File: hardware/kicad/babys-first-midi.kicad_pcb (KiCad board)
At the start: 2 copper layers, 100 x 70 mm, 26 parts, among them J1 BFM:RJ45_THT, J2 Connector_Audio:TRS_3.5mm_Hor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, Q1 Package_TO_SOT_THT:TO-220-3_V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, Q2 Package_TO_SOT_THT:TO-220-3_V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, Q3 Package_TO_SOT_THT:TO-220-3_V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, Q4 Package_TO_SOT_THT:TO-220-3_V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, Q5 Package_TO_SOT_THT:TO-220-3_V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, U1 Pimoroni Tiny 2350

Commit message: Rotate Tiny 2350 USB-C toward right edge
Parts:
- turned U1 to 90 degrees
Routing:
- net 3V3: track 216.9 -> 181.9 mm
- net ADC_OCTAVE: track 85.1 -> 57.0 mm
- net KEY_G: track 61.4 -> 38.2 mm
- net KEY_F: track 52.9 -> 29.7 mm
- net KEY_E: track 44.4 -> 21.3 mm
- net KEY_D: track 52.4 -> 29.2 mm
- net KEY_C: track 60.8 -> 37.6 mm
- net GND: track 323.8 -> 301.7 mm
- net ADC_SCALE: track 96.0 -> 79.5 mm
- net MIDI_TX: track 27.2 -> 22.0 mm
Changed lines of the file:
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@@
     (pad "2" thru_hole circle (at 5.08 0) (size 2.2 2.2) (drill 1) (layers "*.Cu" "*.Mask") (net 18 "KEY_G"))
   )
-  (footprint "BFM:Pimoroni_Tiny2350_2x8_Header" (layer "F.Cu") (at 94 50)
+  (footprint "BFM:Pimoroni_Tiny2350_2x8_Header" (layer "F.Cu") (at 94 50 90)
     (property "Reference" "U1" (at 0 -12.5 0) (layer "F.SilkS") (effects (font (size 1 1) (thickness 0.15))))
     (property "Value" "Pimoroni Tiny 2350" (at 0 12.5 0) (layer "F.SilkS") (effects (font (size 1 1) (thickness 0.15))))
@@
   (segment (start 81 29.5) (end 81 28) (width 0.45) (layer "F.Cu") (net 2))
   (segment (start 81 28) (end 65.92 28) (width 0.45) (layer "F.Cu") (net 2))
-  (segment (start 101.62 53.81) (end 96.62 73) (width 0.45) (layer "F.Cu") (net 2))
   (segment (start 96.62 73) (end 95.92 73) (width 0.45) (layer "F.Cu") (net 2))
   (segment (start 60.54 82) (end 96.62 82) (width 0.45) (layer "F.Cu") (net 1))
@@
   (segment (start 76.08 32) (end 79 32) (width 0.45) (layer "F.Cu") (net 14))
   (segment (start 79 32) (end 79 48.65) (width 0.45) (layer "F.Cu") (net 14))
-  (segment (start 79 48.65) (end 101.62 43.65) (width 0.45) (layer "F.Cu") (net 14))
   (segment (start 76.08 43) (end 79 43) (width 0.45) (layer "F.Cu") (net 15))
   (segment (start 79 43) (end 79 51.19) (width 0.45) (layer "F.Cu") (net 15))
-  (segment (start 79 51.19) (end 101.62 46.19) (width 0.45) (layer "F.Cu") (net 15))
   (segment (start 76.08 54) (end 79 54) (width 0.45) (layer "F.Cu") (net 16))
   (segment (start 79 54) (end 79 53.73) (width 0.45) (layer "F.Cu") (net 16))
-  (segment (start 79 53.73) (end 101.62 48.73) (width 0.45) (layer "F.Cu") (net 16))
   (segment (start 76.08 65) (end 79 65) (width 0.45) (layer "F.Cu") (net 17))
   (segment (start 79 65) (end 79 56.27) (width 0.45) (layer "F.Cu") (net 17))
-  (segment (start 79 56.27) (end 101.62 51.27) (width 0.45) (layer "F.Cu") (net 17))
   (segment (start 76.08 76) (end 79 76) (width 0.45) (layer "F.Cu") (net 18))
   (segment (start 79 76) (end 79 58.81) (width 0.45) (layer "F.Cu") (net 18))
-  (segment (start 79 58.81) (end 101.62 53.81) (width 0.45) (layer "F.Cu") (net 18))
-  (segment (start 101.62 41.11) (end 100 46.11) (width 0.45) (layer "F.Cu") (net 19))
   (segment (start 100 46.11) (end 100 64) (width 0.45) (layer "F.Cu") (net 19))
   (segment (start 100 64) (end 95.92 64) (width 0.45) (layer "F.Cu") (net 19))
-  (segment (start 101.62 41.11) (end 84 46.11) (width 0.45) (layer "F.Cu") (net 20))
   (segment (start 84 46.11) (end 84 29.5) (width 0.45) (layer "F.Cu") (net 20))
-  (segment (start 101.62 43.65) (end 102 48.65) (width 0.45) (layer "F.Cu") (net 21))
   (segment (start 102 48.65) (end 102 29.5) (width 0.45) (layer "F.Cu") (net 21))
   (segment (start 106.08 67) (end 110 67) (width 0.45) (layer "F.Cu") (net 22))
@@
   (segment (start 108 73) (end 108 70) (width 0.45) (layer "F.Cu") (net 23))
   (segment (start 108 70) (end 110 70) (width 0.45) (layer "F.Cu") (net 23))
-  (segment (start 86.38 58.89) (end 78 63.89) (width 0.45) (layer "F.Cu") (net 20))
   (segment (start 78 63.89) (end 78 29.5) (width 0.45) (layer "F.Cu") (net 20))
   (segment (start 78 29.5) (end 84 29.5) (width 0.45) (layer "F.Cu") (net 20))
-  (segment (start 86.38 53.81) (end 76 58.81) (width 0.45) (layer "F.Cu") (net 21))
   (segment (start 76 58.81) (end 76 27) (width 0.45) (layer "F.Cu") (net 21))
   (segment (start 76 27) (end 102 27) (width 0.45) (layer "F.Cu") (net 21))
   (segment (start 102 27) (end 102 29.5) (width 0.45) (layer "F.Cu") (net 21))
-  (segment (start 86.38 46.19) (end 72 51.19) (width 0.6) (layer "F.Cu") (net 2))
-  (segment (start 86.38 43.65) (end 74 48.65) (width 0.6) (layer "F.Cu") (net 1))
-  (segment (start 86.38 58.89) (end 81.38 66) (width 0.6) (layer "F.Cu") (net 1))
   (zone (net 1) (net_name "GND") (layer "B.Cu") (hatch edge 0.5)
     (connect_pads (clearance 0.5))

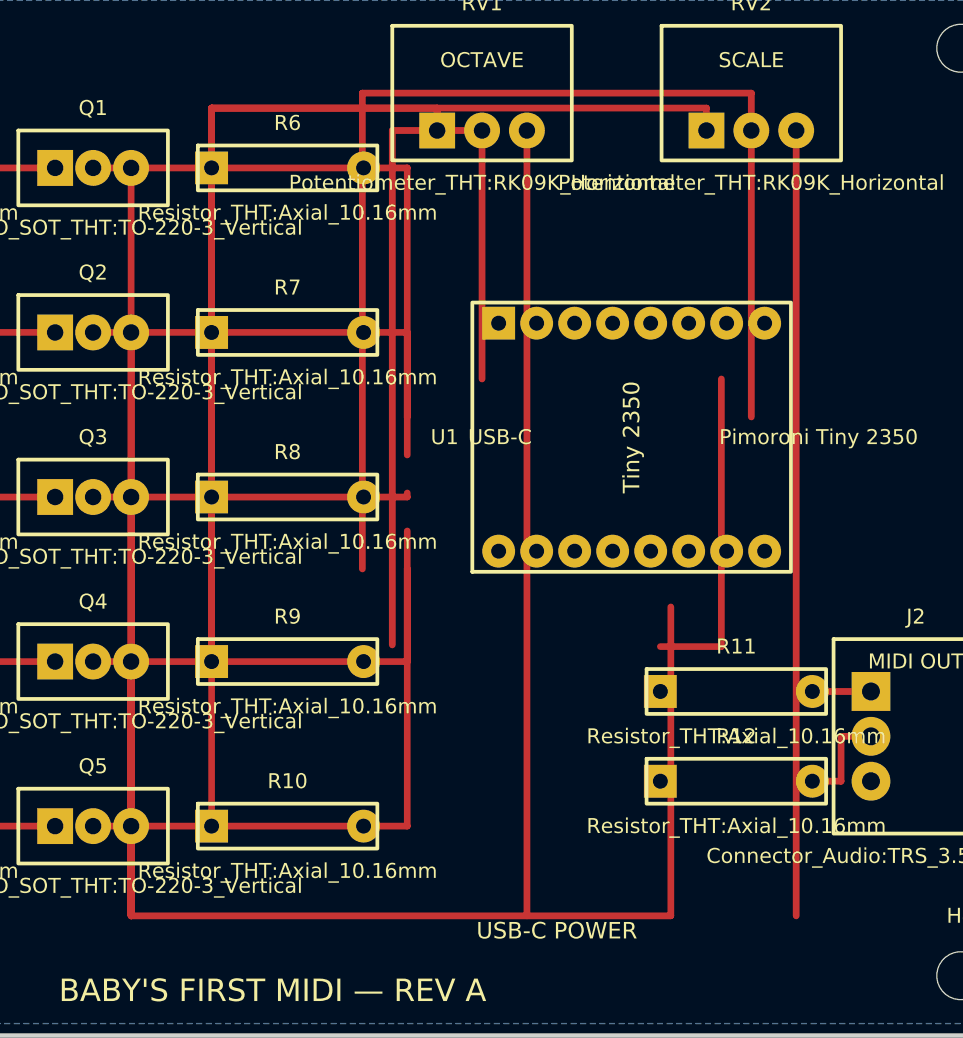
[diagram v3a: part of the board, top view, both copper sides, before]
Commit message: Reroute rotated Tiny 2350 connections
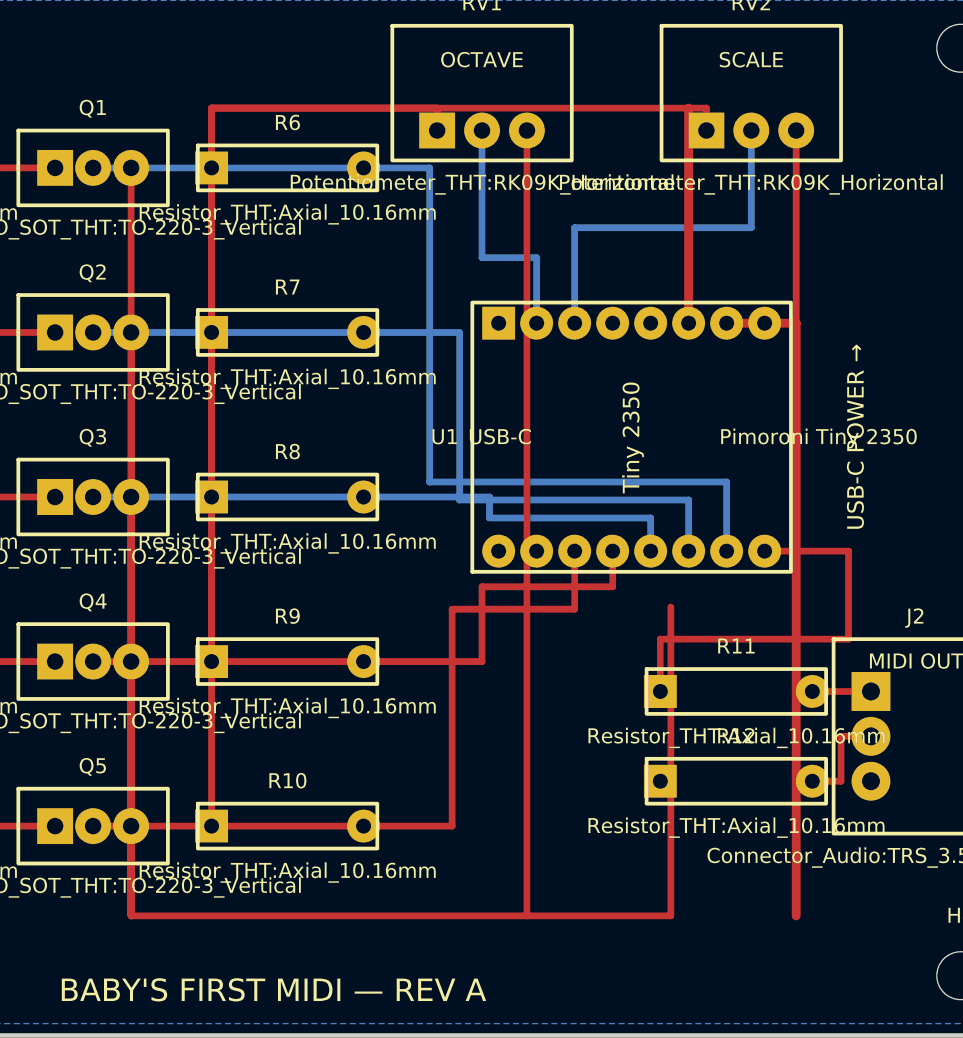
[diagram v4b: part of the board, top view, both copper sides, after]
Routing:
- net ADC_SCALE: track 79.5 -> 24.7 mm
- net GND: track 301.7 -> 346.0 mm
- net ADC_OCTAVE: track 57.0 -> 16.5 mm
- net KEY_C: track 37.6 -> 68.0 mm
- net KEY_D: track 29.2 -> 54.4 mm
- net KEY_E: track 21.3 -> 40.9 mm
- net 3V3: track 181.9 -> 196.2 mm
- net KEY_F: track 29.7 -> 42.1 mm
- net KEY_G: track 38.2 -> 50.6 mm
- net MIDI_TX: track 22.0 -> 27.6 mm
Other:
- board text added: "USB-C POWER →"
- board text removed: "USB-C POWER"
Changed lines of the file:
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@@
   (gr_text "BABY'S FIRST MIDI — REV A" (at 70 87) (layer "F.SilkS") (effects (font (size 1.5 1.5) (thickness 0.25))))
   (gr_text "FPT IN" (at 28 44) (layer "F.SilkS") (effects (font (size 1.2 1.2) (thickness 0.2))))
-  (gr_text "USB-C POWER" (at 89 83) (layer "F.SilkS") (effects (font (size 1.1 1.1) (thickness 0.2))))
+  (gr_text "USB-C POWER →" (at 109 50 90) (layer "F.SilkS") (effects (font (size 1.1 1.1) (thickness 0.2))))
   (segment (start 23 48) (end 34 48) (width 0.45) (layer "F.Cu") (net 3))
   (segment (start 34 48) (end 34 32) (width 0.45) (layer "F.Cu") (net 3))
   (segment (start 34 32) (end 37.92 32) (width 0.45) (layer "F.Cu") (net 3))
   (segment (start 48.08 32) (end 55.46 32) (width 0.45) (layer "F.Cu") (net 9))
-  (segment (start 58 32) (end 76.08 32) (width 0.45) (layer "F.Cu") (net 14))
   (segment (start 65.92 32) (end 65.92 28) (width 0.45) (layer "F.Cu") (net 2))
   (segment (start 60.54 32) (end 60.54 82) (width 0.45) (layer "F.Cu") (net 1))
@@
   (segment (start 34 43) (end 37.92 43) (width 0.45) (layer "F.Cu") (net 4))
   (segment (start 48.08 43) (end 55.46 43) (width 0.45) (layer "F.Cu") (net 10))
-  (segment (start 58 43) (end 76.08 43) (width 0.45) (layer "F.Cu") (net 15))
   (segment (start 65.92 43) (end 65.92 28) (width 0.45) (layer "F.Cu") (net 2))
   (segment (start 60.54 43) (end 60.54 82) (width 0.45) (layer "F.Cu") (net 1))
@@
   (segment (start 34 54) (end 37.92 54) (width 0.45) (layer "F.Cu") (net 5))
   (segment (start 48.08 54) (end 55.46 54) (width 0.45) (layer "F.Cu") (net 11))
-  (segment (start 58 54) (end 76.08 54) (width 0.45) (layer "F.Cu") (net 16))
   (segment (start 65.92 54) (end 65.92 28) (width 0.45) (layer "F.Cu") (net 2))
   (segment (start 60.54 54) (end 60.54 82) (width 0.45) (layer "F.Cu") (net 1))
@@
   (segment (start 34 65) (end 37.92 65) (width 0.45) (layer "F.Cu") (net 6))
   (segment (start 48.08 65) (end 55.46 65) (width 0.45) (layer "F.Cu") (net 12))
-  (segment (start 58 65) (end 76.08 65) (width 0.45) (layer "F.Cu") (net 17))
   (segment (start 65.92 65) (end 65.92 28) (width 0.45) (layer "F.Cu") (net 2))
   (segment (start 60.54 65) (end 60.54 82) (width 0.45) (layer "F.Cu") (net 1))
@@
   (segment (start 34 76) (end 37.92 76) (width 0.45) (layer "F.Cu") (net 7))
   (segment (start 48.08 76) (end 55.46 76) (width 0.45) (layer "F.Cu") (net 13))
-  (segment (start 58 76) (end 76.08 76) (width 0.45) (layer "F.Cu") (net 18))
   (segment (start 65.92 76) (end 65.92 28) (width 0.45) (layer "F.Cu") (net 2))
   (segment (start 60.54 76) (end 60.54 82) (width 0.45) (layer "F.Cu") (net 1))
@@
   (segment (start 87 29.5) (end 87 82) (width 0.45) (layer "F.Cu") (net 1))
   (segment (start 105 29.5) (end 105 82) (width 0.45) (layer "F.Cu") (net 1))
-  (segment (start 76.08 32) (end 79 32) (width 0.45) (layer "F.Cu") (net 14))
-  (segment (start 79 32) (end 79 48.65) (width 0.45) (layer "F.Cu") (net 14))
-  (segment (start 76.08 43) (end 79 43) (width 0.45) (layer "F.Cu") (net 15))
-  (segment (start 79 43) (end 79 51.19) (width 0.45) (layer "F.Cu") (net 15))
-  (segment (start 76.08 54) (end 79 54) (width 0.45) (layer "F.Cu") (net 16))
-  (segment (start 79 54) (end 79 53.73) (width 0.45) (layer "F.Cu") (net 16))
-  (segment (start 76.08 65) (end 79 65) (width 0.45) (layer "F.Cu") (net 17))
-  (segment (start 79 65) (end 79 56.27) (width 0.45) (layer "F.Cu") (net 17))
-  (segment (start 76.08 76) (end 79 76) (width 0.45) (layer "F.Cu") (net 18))
-  (segment (start 79 76) (end 79 58.81) (width 0.45) (layer "F.Cu") (net 18))
-  (segment (start 100 46.11) (end 100 64) (width 0.45) (layer "F.Cu") (net 19))
-  (segment (start 100 64) (end 95.92 64) (width 0.45) (layer "F.Cu") (net 19))
-  (segment (start 84 46.11) (end 84 29.5) (width 0.45) (layer "F.Cu") (net 20))
-  (segment (start 102 48.65) (end 102 29.5) (width 0.45) (layer "F.Cu") (net 21))
   (segment (start 106.08 67) (end 110 67) (width 0.45) (layer "F.Cu") (net 22))
   (segment (start 106.08 73) (end 108 73) (width 0.45) (layer "F.Cu") (net 23))
   (segment (start 108 73) (end 108 70) (width 0.45) (layer "F.Cu") (net 23))
   (segment (start 108 70) (end 110 70) (width 0.45) (layer "F.Cu") (net 23))
-  (segment (start 78 63.89) (end 78 29.5) (width 0.45) (layer "F.Cu") (net 20))
-  (segment (start 78 29.5) (end 84 29.5) (width 0.45) (layer "F.Cu") (net 20))
-  (segment (start 76 58.81) (end 76 27) (width 0.45) (layer "F.Cu") (net 21))
-  (segment (start 76 27) (end 102 27) (width 0.45) (layer "F.Cu") (net 21))
-  (segment (start 102 27) (end 102 29.5) (width 0.45) (layer "F.Cu") (net 21))
+  (segment (start 58 32) (end 76.08 32) (width 0.45) (layer "B.Cu") (net 14))
+  (segment (start 76.08 32) (end 80.5 32) (width 0.45) (layer "B.Cu") (net 14))
+  (segment (start 80.5 32) (end 80.5 53) (width 0.45) (layer "B.Cu") (net 14))
+  (segment (start 80.5 53) (end 100.35 53) (width 0.45) (layer "B.Cu") (net 14))
+  (segment (start 100.35 53) (end 100.35 57.62) (width 0.45) (layer "B.Cu") (net 14))
+  (segment (start 58 43) (end 76.08 43) (width 0.45) (layer "B.Cu") (net 15))
+  (segment (start 76.08 43) (end 82.5 43) (width 0.45) (layer "B.Cu") (net 15))
+  (segment (start 82.5 43) (end 82.5 54.2) (width 0.45) (layer "B.Cu") (net 15))
+  (segment (start 82.5 54.2) (end 97.81 54.2) (width 0.45) (layer "B.Cu") (net 15))
+  (segment (start 97.81 54.2) (end 97.81 57.62) (width 0.45) (layer "B.Cu") (net 15))
+  (segment (start 58 54) (end 76.08 54) (width 0.45) (layer "B.Cu") (net 16))
+  (segment (start 76.08 54) (end 84.5 54) (width 0.45) (layer "B.Cu") (net 16))
+  (segment (start 84.5 54) (end 84.5 55.4) (width 0.45) (layer "B.Cu") (net 16))
+  (segment (start 84.5 55.4) (end 95.27 55.4) (width 0.45) (layer "B.Cu") (net 16))
+  (segment (start 95.27 55.4) (end 95.27 57.62) (width 0.45) (layer "B.Cu") (net 16))
+  (segment (start 58 65) (end 76.08 65) (width 0.45) (layer "F.Cu") (net 17))
+  (segment (start 76.08 65) (end 84 65) (width 0.45) (layer "F.Cu") (net 17))
+  (segment (start 84 65) (end 84 60) (width 0.45) (layer "F.Cu") (net 17))
+  (segment (start 84 60) (end 92.73 60) (width 0.45) (layer "F.Cu") (net 17))
+  (segment (start 92.73 60) (end 92.73 57.62) (width 0.45) (layer "F.Cu") (net 17))
+  (segment (start 58 76) (end 76.08 76) (width 0.45) (layer "F.Cu") (net 18))
+  (segment (start 76.08 76) (end 82 76) (width 0.45) (layer "F.Cu") (net 18))
+  (segment (start 82 76) (end 82 61.5) (width 0.45) (layer "F.Cu") (net 18))
+  (segment (start 82 61.5) (end 90.19 61.5) (width 0.45) (layer "F.Cu") (net 18))
+  (segment (start 90.19 61.5) (end 90.19 57.62) (width 0.45) (layer "F.Cu") (net 18))
+  (segment (start 102.89 57.62) (end 108.5 57.62) (width 0.45) (layer "F.Cu") (net 19))
+  (segment (start 108.5 57.62) (end 108.5 63.5) (width 0.45) (layer "F.Cu") (net 19))
+  (segment (start 108.5 63.5) (end 95.92 63.5) (width 0.45) (layer "F.Cu") (net 19))
+  (segment (start 95.92 63.5) (end 95.92 67) (width 0.45) (layer "F.Cu") (net 19))
+  (segment (start 84 29.5) (end 84 38) (width 0.45) (layer "B.Cu") (net 20))
+  (segment (start 84 38) (end 87.65 38) (width 0.45) (layer "B.Cu") (net 20))
+  (segment (start 87.65 38) (end 87.65 42.38) (width 0.45) (layer "B.Cu") (net 20))
+  (segment (start 102 29.5) (end 102 36) (width 0.45) (layer "B.Cu") (net 21))
+  (segment (start 102 36) (end 90.19 36) (width 0.45) (layer "B.Cu") (net 21))
+  (segment (start 90.19 36) (end 90.19 42.38) (width 0.45) (layer "B.Cu") (net 21))
+  (segment (start 97.81 42.38) (end 97.81 28) (width 0.6) (layer "F.Cu") (net 2))
+  (segment (start 100.35 42.38) (end 105 42.38) (width 0.6) (layer "F.Cu") (net 1))
+  (segment (start 105 42.38) (end 105 82) (width 0.6) (layer "F.Cu") (net 1))
   (zone (net 1) (net_name "GND") (layer "B.Cu") (hatch edge 0.5)
     (connect_pads (clearance 0.5))

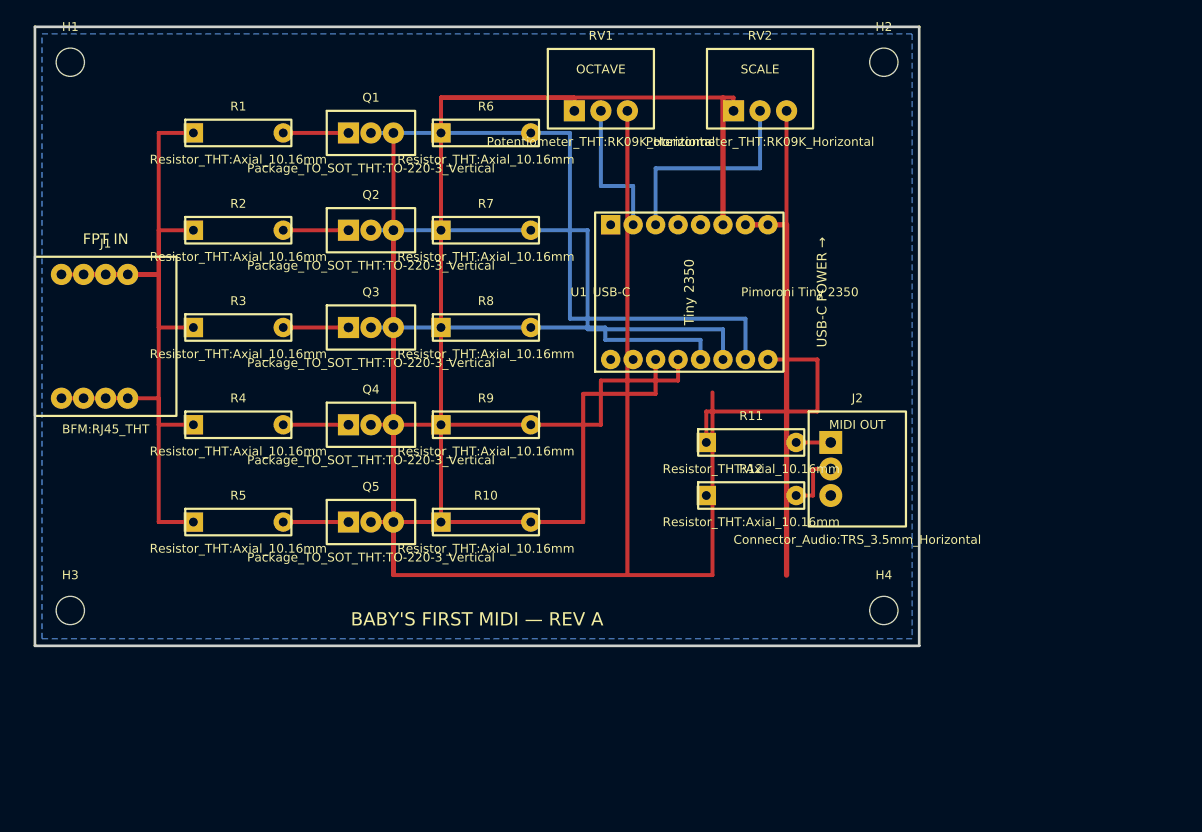
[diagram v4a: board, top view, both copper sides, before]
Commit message: Rebuild PCB routing for DRC clearance
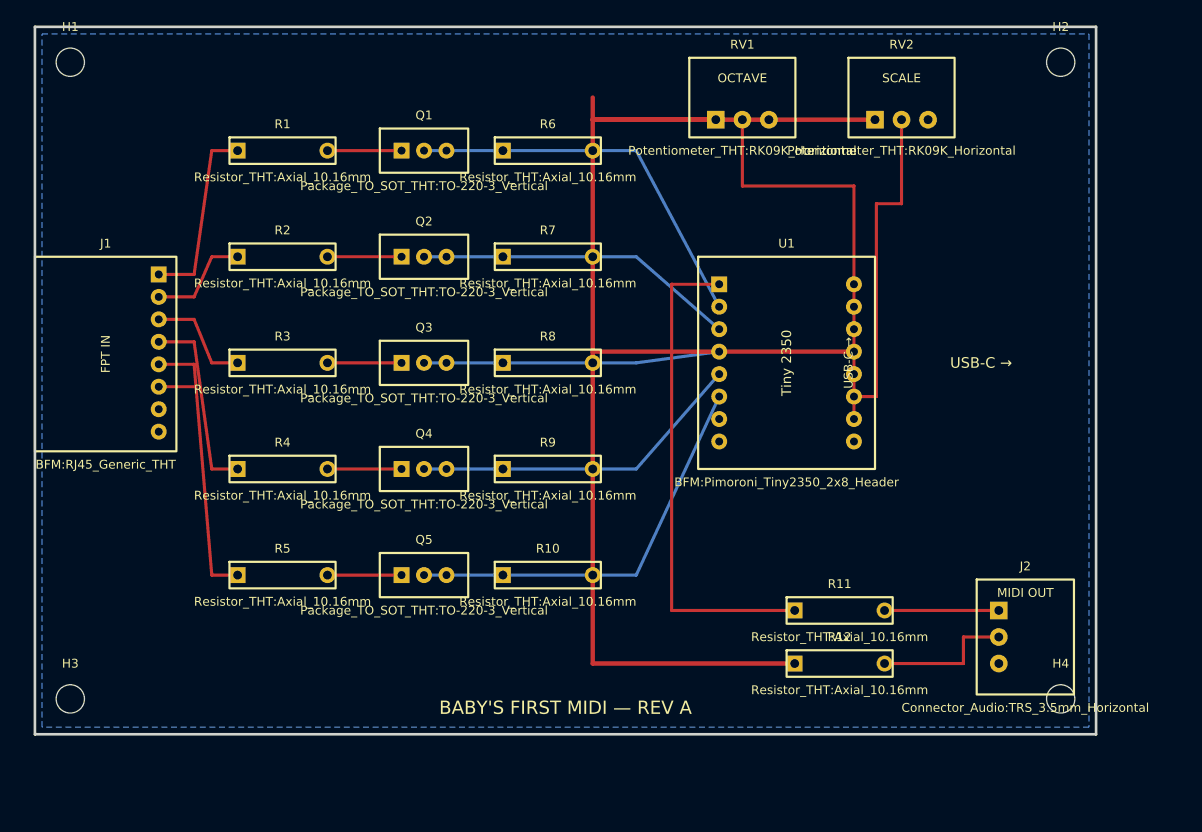
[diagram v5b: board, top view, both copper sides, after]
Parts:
- J1: value BFM:RJ45_THT -> BFM:RJ45_Generic_THT; footprint BFM:RJ45_THT -> BFM:RJ45_Generic_THT
- U1: value Pimoroni Tiny 2350 -> BFM:Pimoroni_Tiny2350_2x8_Header
- moved J2 26.9 mm to (132.0, 89.0)
- moved H4 22.4 mm to (136.0, 96.0)
- moved R11 21.5 mm to (111.0, 86.0)
- moved R12 21.5 mm to (111.0, 92.0)
- moved H2 20.0 mm to (136.0, 24.0)
- moved RV1 16.0 mm to (100.0, 28.0)
- moved RV2 16.0 mm to (118.0, 28.0)
- moved U1 13.6 mm to (105.0, 58.0), turned to 0 degrees
- moved H3 10.0 mm to (24.0, 96.0)
- moved R10 9.22 mm to (78.0, 82.0)
- moved R9 8.60 mm to (78.0, 70.0)
- moved Q5 8.49 mm to (64.0, 82.0)
- moved R8 8.06 mm to (78.0, 58.0)
- moved Q4 7.81 mm to (64.0, 70.0)
- moved R5 7.81 mm to (48.0, 82.0)
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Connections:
- R10 pad 1: 3V3 -> KEY_G
- R10 pad 2: KEY_G -> 3V3
- R6 pad 1: 3V3 -> KEY_C
- R6 pad 2: KEY_C -> 3V3
- R7 pad 1: 3V3 -> KEY_D
- R7 pad 2: KEY_D -> 3V3
- R8 pad 1: 3V3 -> KEY_E
- R8 pad 2: KEY_E -> 3V3
- R9 pad 1: 3V3 -> KEY_F
- R9 pad 2: KEY_F -> 3V3
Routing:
- net GND: track 346.0 -> 0.00 mm
- net 3V3: track 196.2 -> 162.2 mm
- net ADC_OCTAVE: track 16.5 -> 46.5 mm
- net MIDI_TX: track 27.6 -> 56.2 mm
- net KEY_C: track 68.0 -> 44.0 mm
- net KEY_D: track 54.4 -> 36.5 mm
- net ADC_SCALE: track 24.7 -> 36.7 mm
- net FPT_C: track 30.9 -> 21.1 mm
- net MIDI_TIP: track 3.92 -> 12.9 mm
- net MIDI_RING: track 6.92 -> 15.9 mm
- net KEY_E: track 40.9 -> 33.5 mm
- net FPT_D: track 17.4 -> 11.9 mm
- net KEY_G: track 50.6 -> 46.3 mm
- net FPT_COMMON: track 0.00 -> 4.00 mm
- net KEY_F: track 42.1 -> 38.3 mm
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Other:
- board size 100 x 70 mm -> 120 x 80 mm
- board text added: "USB-C →"
- board text removed: "FPT IN"
- board text removed: "USB-C POWER →"
